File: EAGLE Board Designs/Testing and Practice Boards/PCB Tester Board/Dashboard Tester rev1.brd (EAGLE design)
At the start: 160 x 100 mm, 32 parts, among them J1 CONNECTOR-CAN_NF_T_V_BLACK, J2 CONNECTOR-6_NF_T_V_BLACK, J3 CONNECTOR-8_NF_T_V_BLACK, Q1 TRANSISTOR_N_MOS_PMV15ENEA, Q10 TRANSISTOR_N_MOS_PMV15ENEA, Q11 TRANSISTOR_P_MOS_SOT23_SI2369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, Q2 TRANSISTOR_N_MOS_PMV15ENEA, Q3 TRANSISTOR_N_MOS_PMV15ENEA, Q4 TRANSISTOR_N_MOS_PMV15ENEA, Q5 TRANSISTOR_N_MOS_PMV15ENEA, Q6 TRANSISTOR_N_MOS_PMV15ENEA, Q7 TRANSISTOR_P_MOS_SOT23_SI2369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, Q8 TRANSISTOR_N_MOS_PMV15ENEA, Q9 TRANSISTOR_P_MOS_SOT23_SI2369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, U1 TEENSY_3.5, U2 CAN_TRANSCIEVER_TCAN1051HQV-Q1, U3 VOLTAGE_REGULATOR_OKI-78SR_5V

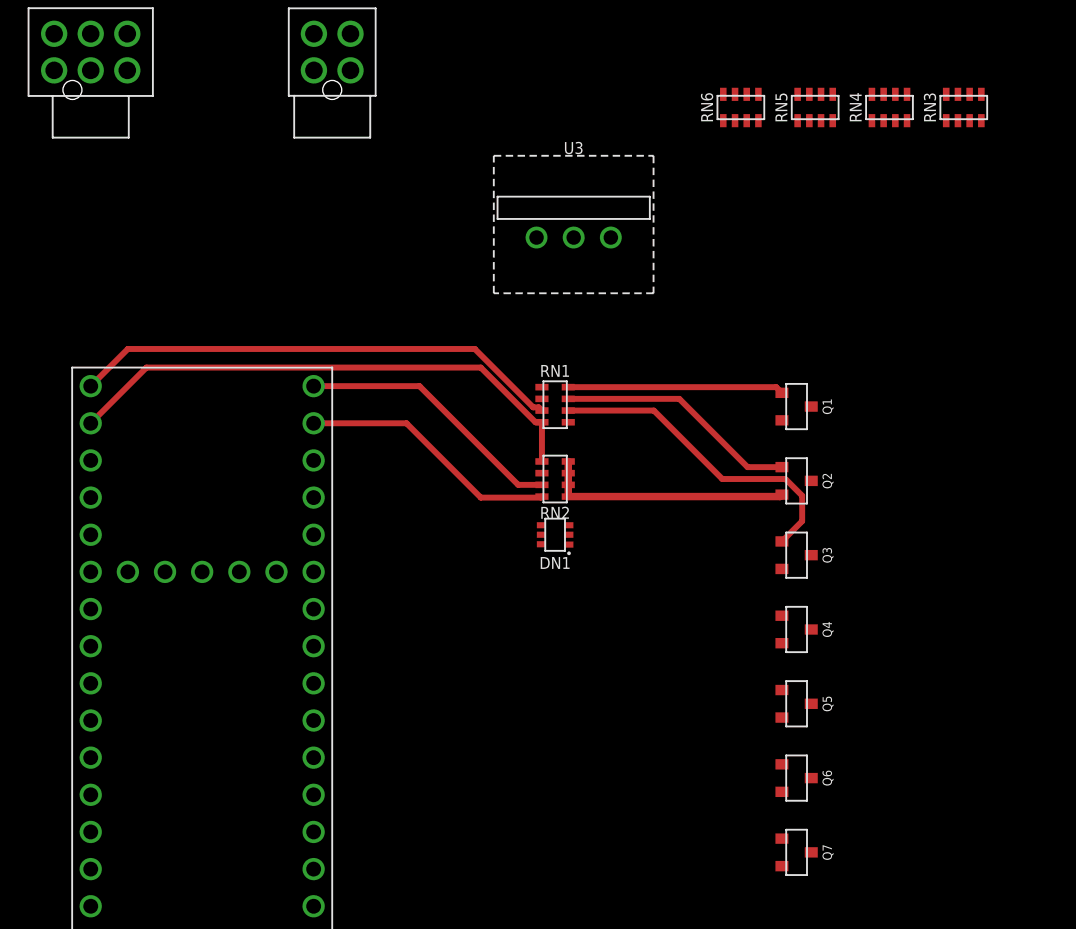
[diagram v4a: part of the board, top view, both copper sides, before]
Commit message: Rearranged control-teensy connections
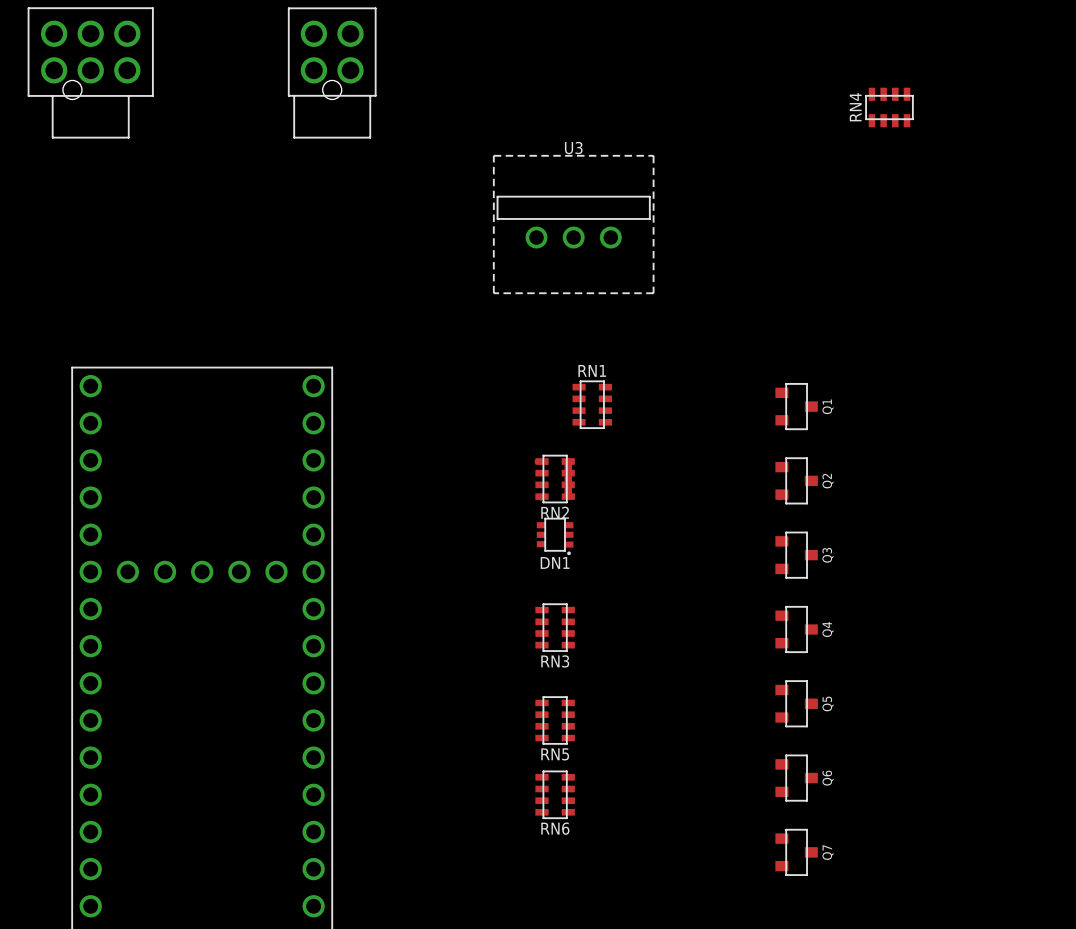
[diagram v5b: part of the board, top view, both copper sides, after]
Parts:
- moved RN6 48.7 mm to (44.5, 43.2), turned to 90 degrees
- moved RN5 45.5 mm to (44.5, 48.3), turned to 90 degrees
- moved RN3 45.2 mm to (44.5, 54.6), turned to 90 degrees
- moved RN1 2.54 mm to (47.0, 69.8)
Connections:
- removed net N$5: U1.D36
- net BTN_LC_CTRL: now also U1.D28; no longer U1.D35
- net BTN_MARK_CTRL: now also U1.D32; no longer U1.D31
- net BTN_MC_CYCLE_CTRL: now also U1.D31; no longer U1.D32
- net BTN_MODE_CTRL: now also U1.D30; no longer U1.D33
- net BTN_START_CTRL: now also U1.D29; no longer U1.D34
- net DASH_12V_CTRL: now also U1.D27
- net SHUTDOWN_H_CTRL: now also U1.D25; no longer U1.D38
- net SSOK_CTRL: now also U1.D26; no longer U1.D37
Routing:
- net BTN_START_CTRL: track 36.7 -> 0.30 mm
- net BTN_MODE_CTRL: track 33.6 -> 0.00 mm
- net N$6: track 22.1 -> 0.00 mm
- net BTN_MC_CYCLE_CTRL: track 18.4 -> 0.00 mm
- net BTN_MARK_CTRL: track 17.7 -> 0.10 mm
- net N$4: track 16.5 -> 0.00 mm
- net N$1: track 14.8 -> 0.00 mm
- net GND: track 17.1 -> 2.59 mm

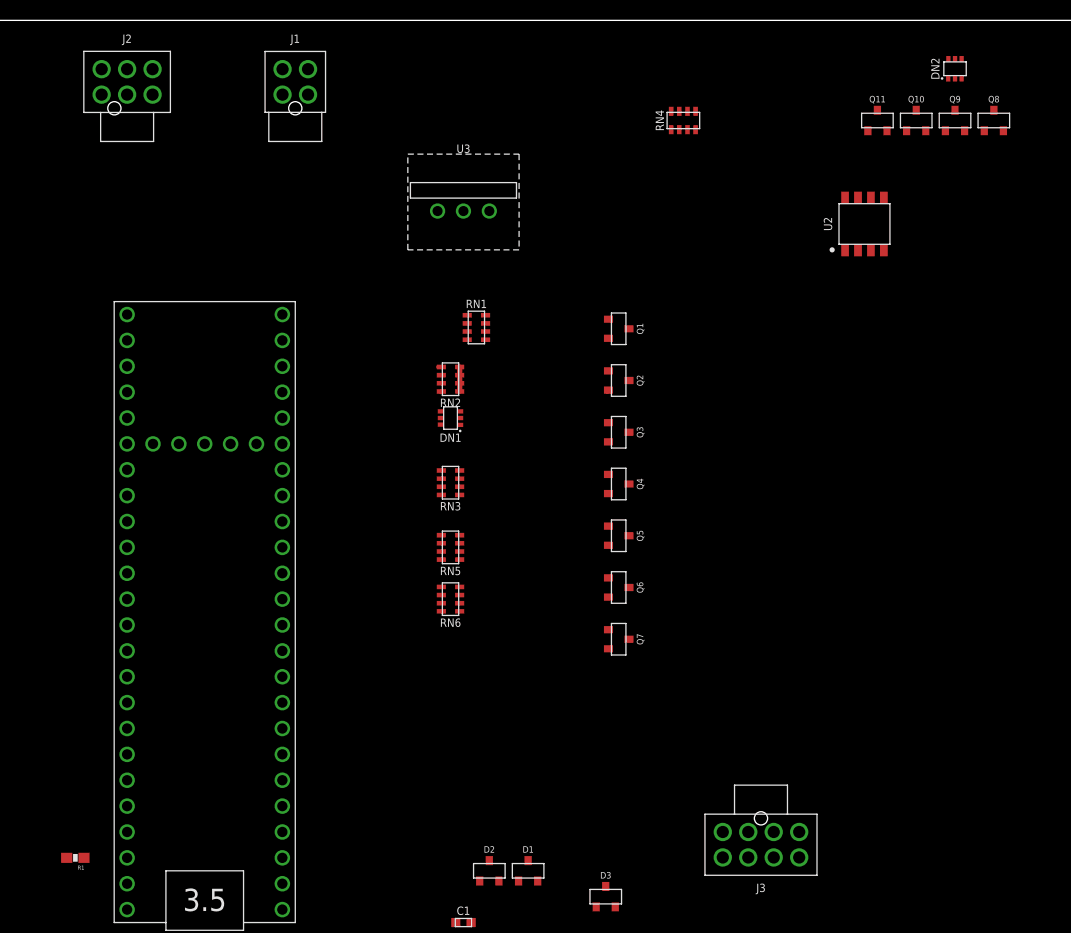
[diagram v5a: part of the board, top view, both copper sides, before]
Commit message: Routed control signals
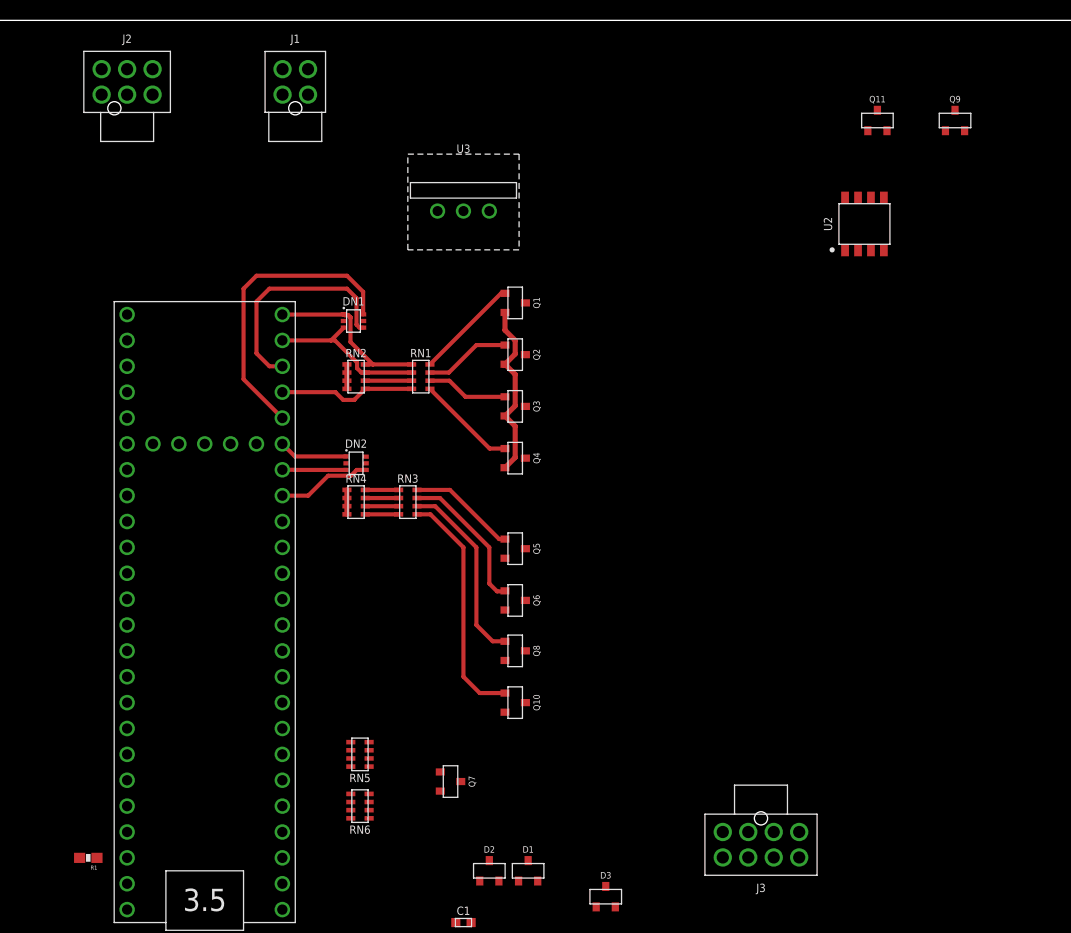
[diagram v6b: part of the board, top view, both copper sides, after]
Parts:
- moved DN2 70.4 mm to (35.2, 56.5), turned to 270 degrees
- moved Q8 70.1 mm to (50.8, 38.1), turned to 270 degrees
- moved Q10 69.4 mm to (50.8, 33.0), turned to 270 degrees
- moved RN4 49.4 mm to (35.2, 52.7), turned to 270 degrees
- moved RN6 22.2 mm to (35.6, 22.9)
- moved RN5 22.2 mm to (35.6, 27.9)
- moved Q7 21.6 mm to (44.5, 25.3)
- moved DN1 13.5 mm to (34.9, 70.5), turned to 270 degrees
- moved Q1 10.5 mm to (50.8, 72.3)
- moved Q2 10.5 mm to (50.8, 67.2)
- moved Q3 10.5 mm to (50.8, 62.1)
- moved Q4 10.5 mm to (50.8, 57.0)
- moved Q5 10.2 mm to (50.8, 48.1)
- moved Q6 10.2 mm to (50.8, 43.1)
- moved RN2 9.27 mm to (35.2, 65.0), turned to 270 degrees
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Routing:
- net BTN_LC_CTRL: track 0.00 -> 32.7 mm
- net BTN_MODE_CTRL: track 0.00 -> 26.8 mm
- net N$18: track 0.00 -> 23.3 mm
- net GND: track 2.59 -> 22.7 mm
- net N$13: track 0.00 -> 18.6 mm
- net BTN_MARK_CTRL: track 0.10 -> 17.0 mm
- net BTN_MC_CYCLE_CTRL: track 0.00 -> 16.1 mm
- net N$3: track 0.00 -> 14.5 mm
- net BTN_START_CTRL: track 0.30 -> 13.5 mm
- net SHUTDOWN_H_CTRL: track 0.00 -> 12.5 mm
- net N$10: track 0.00 -> 10.6 mm
- net N$1: track 0.00 -> 10.3 mm
- net DASH_12V_CTRL: track 0.00 -> 10.1 mm
- net N$8: track 0.00 -> 9.80 mm
- net SSOK_CTRL: track 0.00 -> 9.58 mm
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
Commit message: Continuing trace work
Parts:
- moved J3 34.7 mm to (88.9, 52.1), turned to 180 degrees
- moved Q7 21.8 mm to (57.1, 43.1)
- moved RN3 2.54 mm to (40.3, 50.2)
- moved RN4 2.54 mm to (35.2, 50.2)
- moved Q6 2.29 mm to (50.8, 45.3)
- moved Q8 2.29 mm to (50.8, 40.4)
- moved Q10 2.29 mm to (50.8, 35.3)
- moved Q5 2.29 mm to (50.8, 50.4)
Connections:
- removed net BUZZER_CTRL: J3.4
- net BTN_LAUNCH_CONTROL: now also J3.4; no longer J3.7
- net BTN_MARK: now also J3.8; no longer J3.2
- net BTN_MC_CYCLE: now also J3.7; no longer J3.3
- net BTN_MODE: now also J3.6; no longer J3.5
- net BTN_START: now also J3.5; no longer J3.6
- net DASH_12V: now also J3.1
- net SHUTDOWN_H_OUT: now also J3.3
- net SSOK_OUT: now also J3.2
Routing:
- net GND: track 22.7 -> 76.6 mm
- net BTN_MARK: track 0.00 -> 50.6 mm
- net BTN_START_CTRL: track 13.5 -> 59.5 mm
- net BTN_MC_CYCLE: track 0.00 -> 44.7 mm
- net N$7: track 0.00 -> 40.5 mm
- net BTN_MODE: track 0.00 -> 39.0 mm
- net BTN_START: track 0.00 -> 34.4 mm
- net SSOK_CTRL: track 9.58 -> 30.4 mm
- net DASH_12V_CTRL: track 10.1 -> 25.9 mm
- net BTN_LC_CTRL: track 32.7 -> 47.5 mm, vias 0 -> 1
- net BTN_MODE_CTRL: track 26.8 -> 36.4 mm
- net N$18: track 23.3 -> 16.9 mm
- net SHUTDOWN_H_CTRL: track 12.5 -> 18.7 mm
- net N$13: track 18.6 -> 13.8 mm
- net N$3: track 14.5 -> 10.5 mm
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
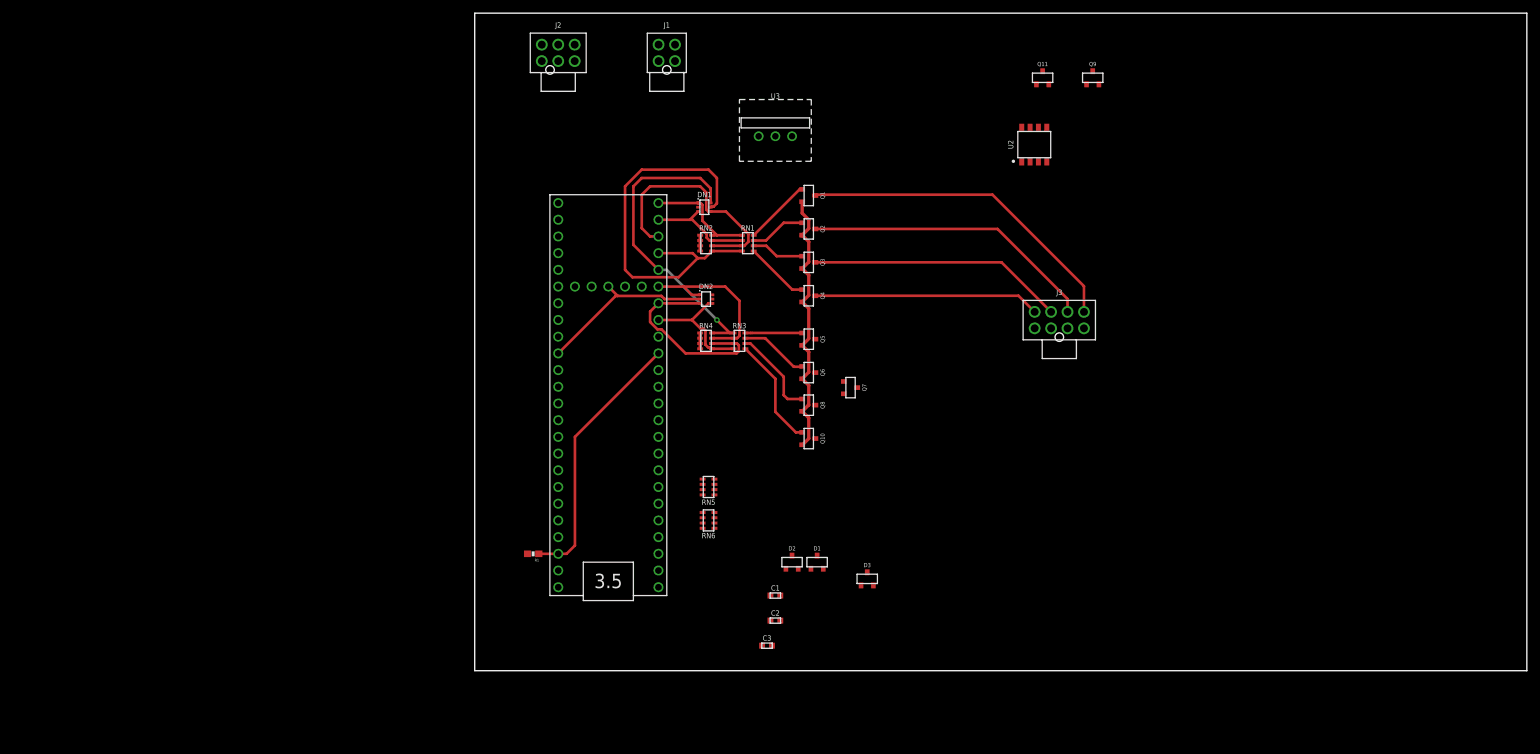
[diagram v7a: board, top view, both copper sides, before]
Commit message: Rearranged pin config
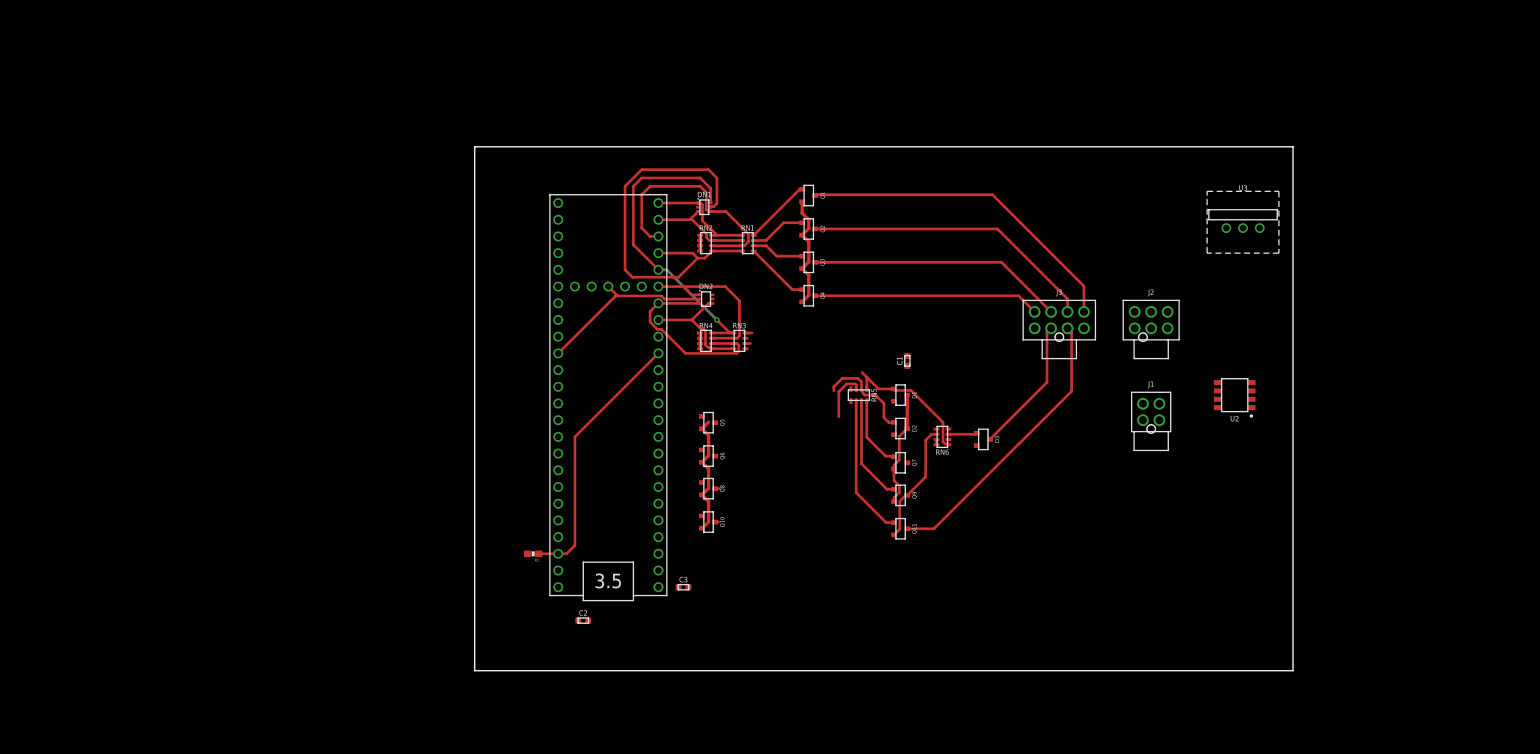
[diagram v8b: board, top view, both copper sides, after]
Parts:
- moved J2 98.9 mm to (102.9, 52.1)
- moved J1 91.7 mm to (102.9, 38.1)
- moved U3 72.5 mm to (116.8, 67.3)
- moved Q11 71.9 mm to (64.8, 21.6), turned to 270 degrees
- moved Q9 69.9 mm to (64.8, 26.7), turned to 270 degrees
- moved U2 48.8 mm to (115.6, 41.9), turned to 90 degrees
- moved C1 40.9 mm to (65.8, 47.1), turned to 90 degrees
- moved RN6 37.8 mm to (71.1, 35.6)
- moved C2 29.2 mm to (16.5, 7.62)
- moved D1 28.4 mm to (64.8, 41.9), turned to 270 degrees
- moved D3 27.6 mm to (77.3, 35.2), turned to 270 degrees
- moved RN5 26.8 mm to (58.4, 41.9), turned to 180 degrees
- moved D2 26.2 mm to (64.8, 36.8), turned to 270 degrees
- moved Q10 19.8 mm to (35.6, 22.6)
- moved Q5 19.8 mm to (35.6, 37.7)
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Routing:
- net SHUTDOWN_H_OUT: track 0.00 -> 43.5 mm
- net SSOK_OUT: track 0.00 -> 39.3 mm
- net N$21: track 0.00 -> 21.6 mm
- net N$19: track 0.00 -> 21.2 mm
- net +12V: track 0.00 -> 18.5 mm
- net N$18: track 16.9 -> 0.00 mm
- net N$15: track 0.00 -> 16.1 mm
- net N$16: track 0.00 -> 15.9 mm
- net N$13: track 13.8 -> 0.77 mm
- net N$22: track 0.00 -> 12.6 mm
- net N$17: track 0.00 -> 10.9 mm
- net N$3: track 10.5 -> 0.07 mm
- net N$10: track 8.64 -> 1.03 mm
- net GND: track 76.6 -> 70.6 mm
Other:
- board size 160 x 100 mm -> 124.4 x 79.7 mm
